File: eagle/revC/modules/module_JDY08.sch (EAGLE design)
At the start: 32 parts

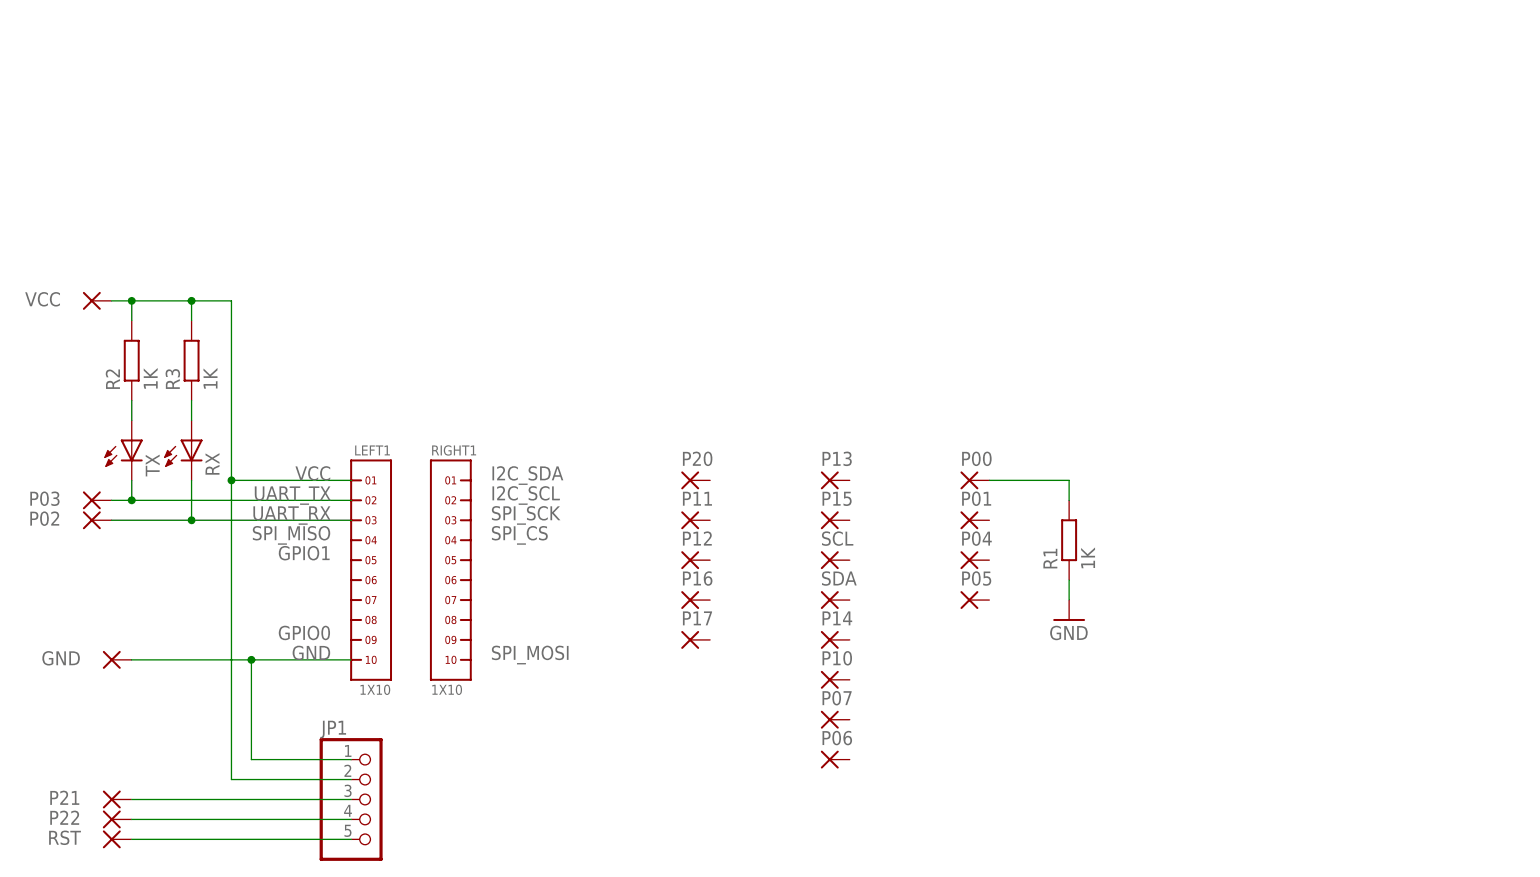
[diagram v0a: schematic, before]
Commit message: Replaced modules with library parts
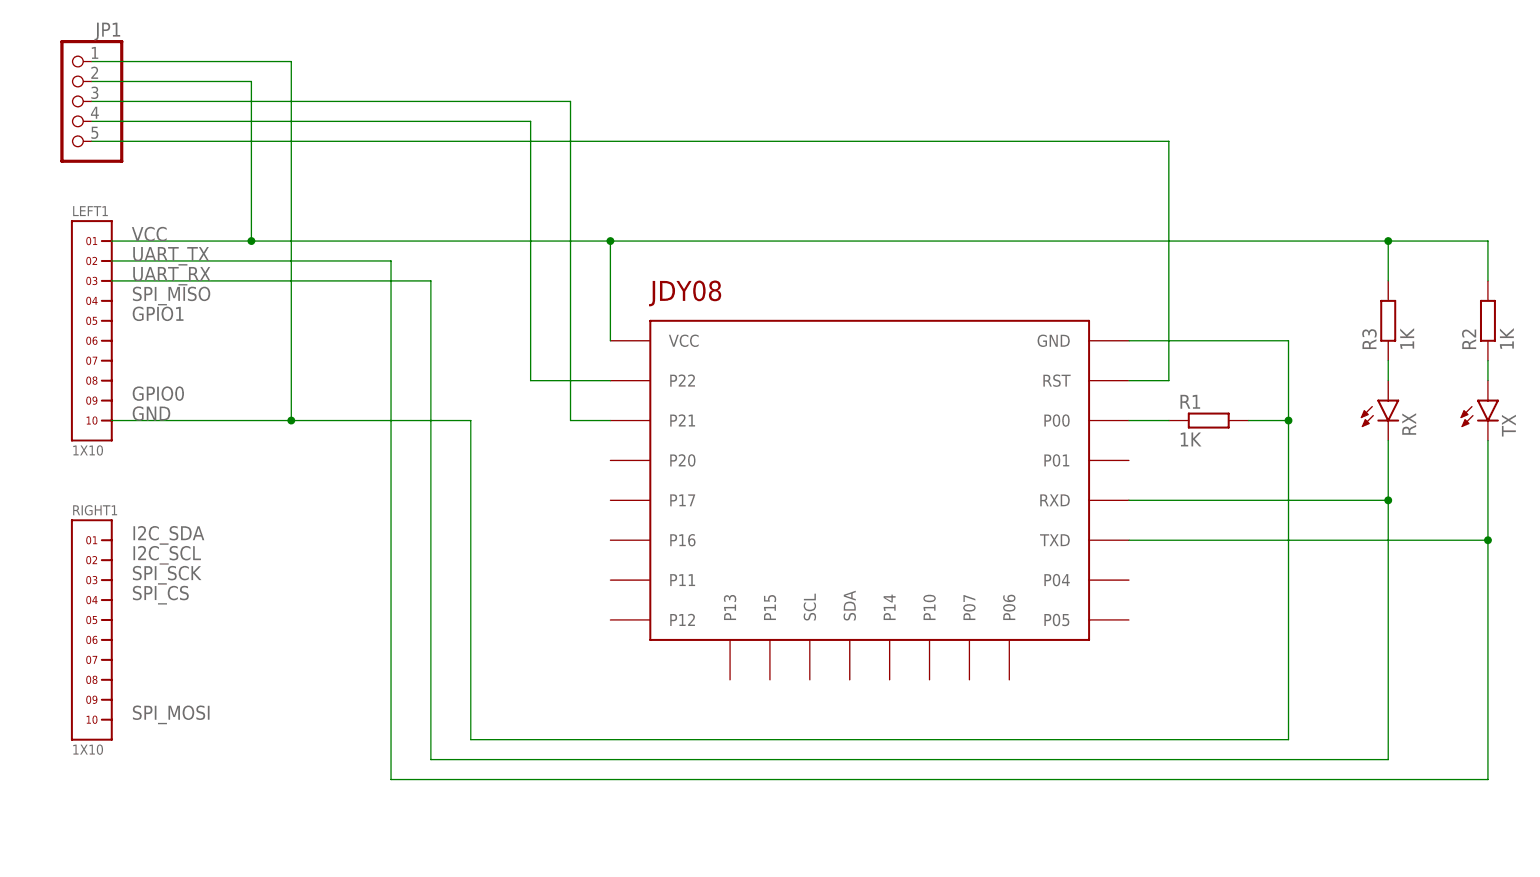
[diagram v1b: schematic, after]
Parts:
- removed GND, P00, P01, P02, P03, P04, P05, P06, P07, P10, P11, P12, P13, P14, P15, P16, P17, P20, P21, P22, RST, SCL, SDA, VCC: (no value), wirepad:SMD1
- added U$1: JDY08, RadioShield:JDY08
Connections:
- removed net N$5: LEFT1.3, P02.P, RX.C
- removed net N$6: LEFT1.2, P03.P, TX.C
- new net N$10: R1.1, U$1.P00
- new net N$11: LEFT1.2, TX.C, U$1.TXD
- net GND: now also R1.2, U$1.GND; no longer GND.P, R1.1
- net N$1: now also U$1.RST; no longer RST.P
- net N$2: now also U$1.P21; no longer P21.P
- net N$3: now also U$1.P22; no longer P22.P
- net N$4: now also LEFT1.3, RX.C, U$1.RXD; no longer P00.P, R1.2
- net VCC: now also U$1.VCC; no longer VCC.P
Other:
- moved on the sheet: JP1, LEFT1, R1, R2, R3, RIGHT1
